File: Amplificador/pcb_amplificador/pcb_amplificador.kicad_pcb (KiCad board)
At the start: 2 copper layers, 196.8 x 88.9 mm, 143 parts, among them CON1 SJ-3523-SMT-TR, J1 Screw_Terminal_01x02, J2 Screw_Terminal_01x02, J3 Screw_Terminal_01x02, J4 Screw_Terminal_01x02, J5 Conn_01x03_Male, J6 Screw_Terminal_01x02, J7 Screw_Terminal_01x02, K1 SANYOU_SRD_Form_B, M1 FDS9934C, M2 FDS9934C, Q1 BC860, Q10 BD139, Q11 BD140, Q12 BD139, Q13 2SA1943-O_Q_, Q14 2SC5200-O_Q, Q15 2SA1943-O_Q_, Q16 2SC5200-O_Q, Q17 2SAR514P5, Q18 BC860, Q19 BC860, Q2 BC860, Q20 2SAR514P5, Q21 2SCR514P5, Q22 2SCR514P5, Q23 2SCR514P5, Q24 2SAR514P5, Q25 2SCR514P5, Q26 BC817, Q27 BC817, Q28 BC807, Q29 BS170, Q3 BC850, Q4 BC850, Q5 BC860, Q6 BC860, Q7 BC850, Q8 2SCR514P5, Q9 2SCR514P5

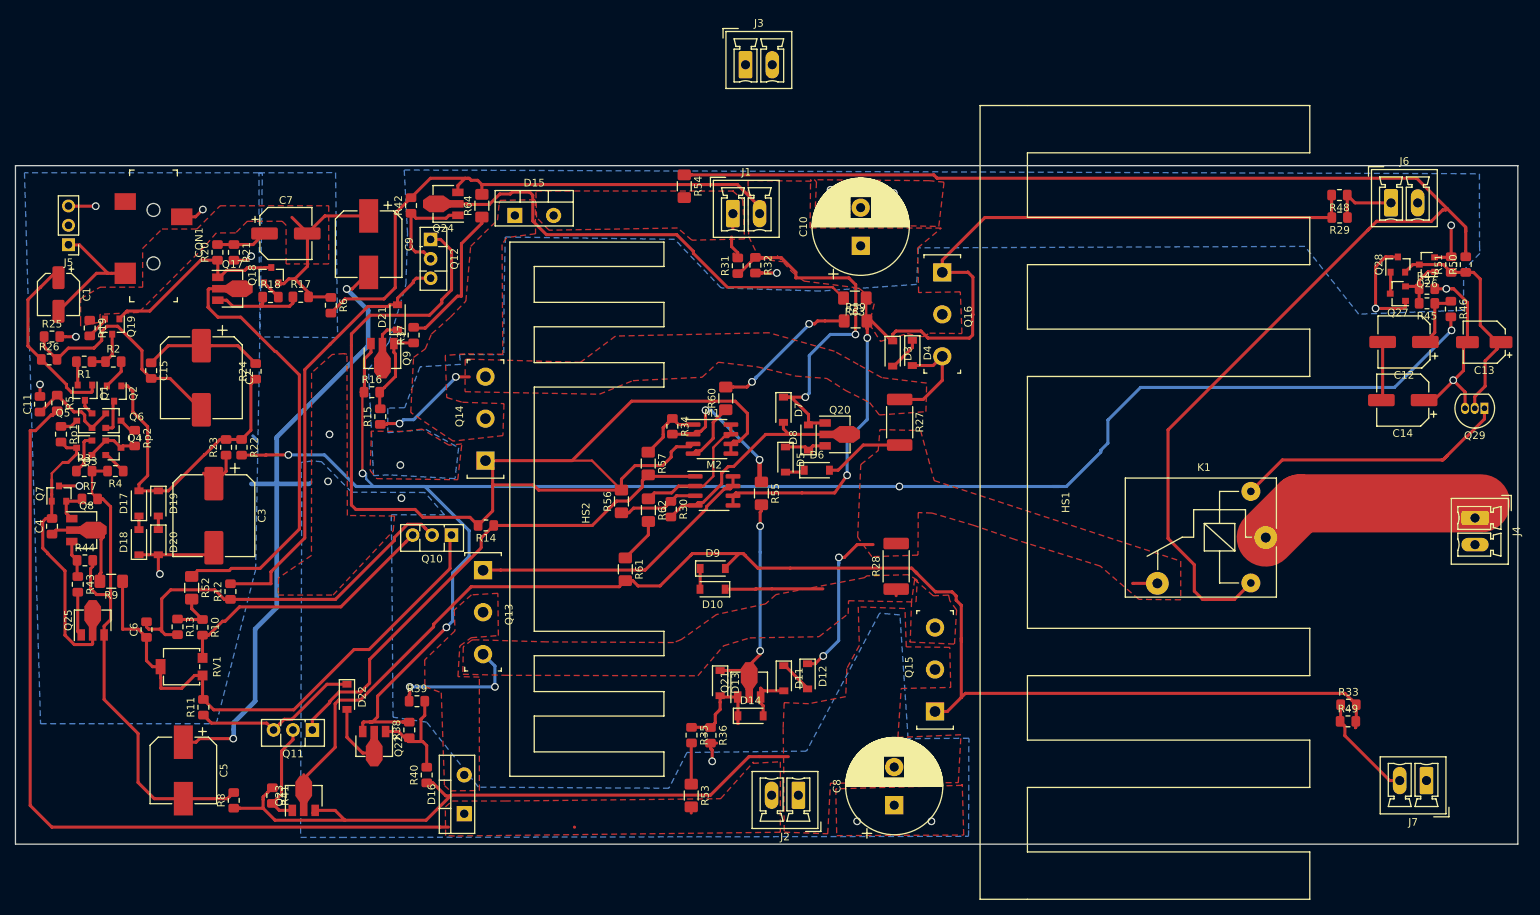
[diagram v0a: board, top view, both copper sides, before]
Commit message: Se mueve el contenido sobre PCB de la rama PCB_review a develop
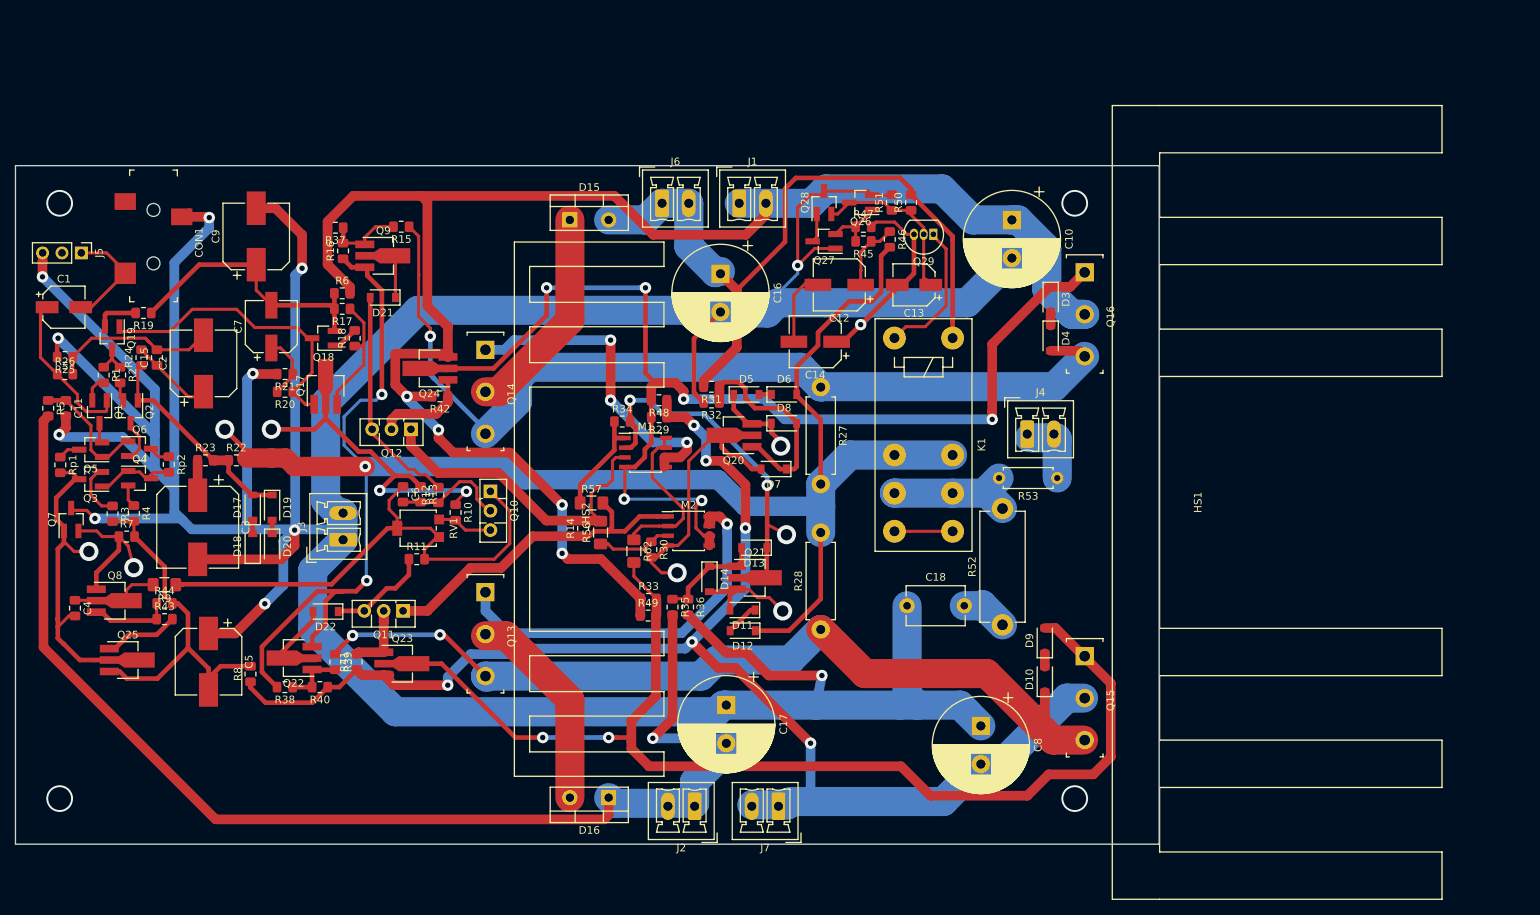
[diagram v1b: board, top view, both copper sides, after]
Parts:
- removed R54, R55, R59, R60, R61, R63, R64: 0, Resistor_SMD:R_1206_3216Metric_Pad1.42x1.75mm_HandSolder
- added C16: 470u, Capacitor_THT:CP_Radial_D12.5mm_P5.00mm, F.Cu at (121.6, 66.2)
- added C17: 470u, Capacitor_THT:CP_Radial_D12.5mm_P5.00mm, F.Cu at (122.3, 122.8)
- added C18: 100n, Capacitor_THT:C_Disc_D7.5mm_W5.0mm_P7.50mm, F.Cu at (146.0, 109.7)
- C2: footprint Capacitor_SMD:CP_Elec_10x10.5 -> Capacitor_SMD:CP_Elec_8x10.5
- K1: value SANYOU_SRD_Form_B -> FINDER-40.11-2016; footprint Relay_THT:Relay_SPST_SANYOU_SRD_Series_Form_B -> Relay_THT:Relay_SPDT_Schrack-RP-II-1-16A-FormC_RM5mm
- Q1, Q18, Q19, Q2, Q26, Q27, Q28, Q3, Q4, Q5, Q6, Q7: footprint Package_TO_SOT_SMD:SOT-23 -> Package_TO_SOT_SMD:SOT-23_Handsoldering
- Q17, Q20, Q21, Q22, Q23, Q24, Q25, Q8, Q9: footprint Package_TO_SOT_SMD:SOT-89-3 -> Package_TO_SOT_SMD:SOT-89-3_Handsoldering
- R27, R28: footprint Resistor_SMD:R_2512_6332Metric_Pad1.52x3.35mm_HandSolder -> Resistor_THT:R_Axial_DIN0411_L9.9mm_D3.6mm_P12.70mm_Horizontal
- R52: value 0 -> 10; footprint Resistor_SMD:R_1206_3216Metric_Pad1.42x1.75mm_HandSolder -> Resistor_THT:R_Axial_DIN0614_L14.3mm_D5.7mm_P15.24mm_Horizontal
- R53: value 0 -> 3.3; footprint Resistor_SMD:R_1206_3216Metric_Pad1.42x1.75mm_HandSolder -> Resistor_THT:R_Axial_DIN0207_L6.3mm_D2.5mm_P7.62mm_Horizontal
- moved R52 106.3 mm to (158.5, 112.2), turned to 90 degrees
- moved J6 95.5 mm to (113.9, 57.0)
- moved R48 93.1 mm to (113.5, 82.8)
- moved R29 92.9 mm to (113.5, 85.0)
- moved R33 92.7 mm to (112.2, 108.8)
- moved R49 92.7 mm to (112.1, 111.0)
- moved J7 85.0 mm to (129.2, 136.0)
- moved J3 81.6 mm to (72.1, 101.1), turned to 90 degrees
- moved C14 77.4 mm to (134.0, 75.1)
- moved Q29 75.7 mm to (149.5, 61.1)
- moved Q28 75.6 mm to (135.2, 56.9)
- moved Q27 75.5 mm to (135.2, 62.0)
- moved C13 75.1 mm to (146.9, 67.7)
- moved Q26 74.6 mm to (140.0, 56.9)
- moved C12 74.4 mm to (137.2, 67.7)
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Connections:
- J1 pad 1: /Vmin -> /Vmax
- J2 pad 1: /-Vmax -> /-Vmin
- J4 pad 2: Net-(J4-Pad2) -> Net-(J4-Pad1)
- J6 pad 1: /-Vmax -> /Vmin
- J6 pad 2: Net-(J6-Pad2) -> /Vmin
- J7 pad 1: Net-(J7-Pad1) -> /-Vmax
- J7 pad 2: /Vmax -> /-Vmax
- M1 pad 2: Net-(M1-Pad2) -> Net-(D13-Pad1)
- M1 pad 4: Net-(M1-Pad4) -> Net-(D3-Pad1)
- Q24 pad 2: Net-(Q24-Pad2) -> Net-(D3-Pad1)
- Q29 pad 1: Net-(K1-Pad2) -> Net-(K1-PadA2)
- R10 pad 1: Net-(R10-Pad1) -> Net-(Q17-Pad2)
- R13 pad 1: Net-(R10-Pad1) -> Net-(Q17-Pad2)
- R34 pad 2: Net-(M1-Pad2) -> Net-(D13-Pad1)
- R35 pad 2: Net-(R35-Pad2) -> /-Vmin
- R37 pad 2: Net-(R37-Pad2) -> /Vmax
- R50 pad 2: Net-(K1-Pad5) -> /Vmin
- R52 pad 1: Net-(Q17-Pad2) -> Net-(C18-Pad2)
- R52 pad 2: Net-(R10-Pad1) -> Net-(K1-Pad11)
- R53 pad 1: Net-(R35-Pad2) -> Net-(J4-Pad1)
- R53 pad 2: /-Vmin -> Net-(K1-Pad11)
- R62 pad 2: Net-(R61-Pad1) -> Net-(D9-Pad2)
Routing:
- net Earth: track 165.8 -> 607.9 mm, vias 23 -> 12
- net Net-(K1-Pad5): track 191.3 -> 0.00 mm
- net /Vmax: track 90.3 -> 218.9 mm, vias 0 -> 4
- net Net-(D4-Pad2): track 29.6 -> 122.8 mm, vias 2 -> 1
- net /-Vmax: track 98.0 -> 189.4 mm, vias 0 -> 6
- net /Vmin: track 5.70 -> 95.6 mm
- net Net-(D10-Pad1): track 32.0 -> 114.8 mm
- net Net-(Q24-Pad2): track 63.3 -> 0.00 mm
- net Net-(M1-Pad3): track 103.6 -> 43.6 mm
- net /-Vmin: track 110.6 -> 165.3 mm, vias 0 -> 1
- net Net-(K1-Pad2): track 36.4 -> 0.00 mm
- net Net-(C6-Pad2): track 51.0 -> 15.4 mm
- net Net-(D9-Pad2): track 187.9 -> 153.1 mm, vias 0 -> 2
- net Net-(D3-Pad1): track 129.2 -> 161.3 mm, vias 2 -> 6
- net Net-(Q10-Pad3): track 36.2 -> 7.30 mm
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- removed copper zone on F.Cu, net /-Vmax
- removed copper zone on F.Cu, net /-Vmin
- removed copper zone on F.Cu, net /VOUT
- removed copper zone on F.Cu, net /Vmax
- removed copper zone on F.Cu, net /Vmin
- removed copper zone on B.Cu, net Earth
- removed copper zone on F.Cu, net Earth
- removed copper zone on F.Cu, net Net-(C7-Pad2)
- removed copper zone on F.Cu, net Net-(D10-Pad1)
- removed copper zone on F.Cu, net Net-(D15-Pad1)
- removed copper zone on F.Cu, net Net-(D16-Pad2)
- removed copper zone on F.Cu, net Net-(D4-Pad2)
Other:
- board size 196.8 x 88.9 mm -> 149.9 x 88.9 mm
- net class Default: clearance 0.4064 -> 0.3048; via_dia 1.016 -> 1.5; via_drill 0.70104 -> 0.7
- rule trace_clearance: 0.4064 -> 0.3048
- rule trace_min: 0.2 -> 0.3048
- rule via_min_drill: 0.3 -> 0.7
- rule via_min_size: 0.4 -> 0.13
